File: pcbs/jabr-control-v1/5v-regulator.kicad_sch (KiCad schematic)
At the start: 0 parts

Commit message: Worked on power and other areas of the schematic
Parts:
- added C1301, C1309, C1310, C1311: 22u, Capacitor_SMD:C_0805_2012Metric, symbol Device:C_Small
- added C1302: 4u7, Capacitor_SMD:C_0805_2012Metric, symbol Device:C_Small
- added C1303, C1312: 2n2, project_footprints:C_0402, symbol Device:C_Small
- added C1304, C1306: 100n, project_footprints:C_0402, symbol Device:C_Small
- added C1305: 2u2, project_footprints:C_0402, symbol Device:C_Small
- added C1307: 1n, project_footprints:C_0402, symbol Device:C_Small
- added C1308: 4p7, project_footprints:C_0402, symbol Device:C_Small
- added C1313: 1u, project_footprints:C_0402, symbol Device:C_Small
- added D2301: PMEG4002EL-QYL, project_footprints:PMEG4002EL-QYL, symbol DIODE:PMEG4002EL-QYL
- added L1301: 74438356018, Inductor_SMD_Wurth:L_Wurth_WE-MAPI-4020, symbol PWR-IND:4020_74438356018
- added Q2602: DMN21D2UFB-7B, project_footprints:DMN21D2UFB7B, symbol MOSFET:DMN21D2UFB-7B
- added R1301, R1306: 12k1, project_footprints:R_0402, symbol Device:R_Small
- added R1302, R1308: 100k, project_footprints:R_0402, symbol Device:R_Small
- added R1303: 22k, project_footprints:R_0402, symbol Device:R_Small
- added R1304: 10k, project_footprints:R_0402, symbol Device:R_Small
- added R1305: 680R, project_footprints:R_0402, symbol Device:R_Small
- added R1307: 33k, project_footprints:R_0402, symbol Device:R_Small
- added TP1301: 1.5mm, TestPoint:TestPoint_Pad_D1.5mm, symbol Connector:TestPoint_Small
- added U1201: TPS259472ARPWR, project_footprints:TPS259472ARPWR, symbol PWR-SWCH:TPS259472ARPWR
- added U1301: MAX20004AFOC/VY+T, project_footprints:MAX20004AFOC_VY+, symbol MAX-SMPS:MAX20004AFOA_VY+T
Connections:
- new net +3V3_AON: R1302.1, R1308.1
- new net +5V: C1309.1, C1310.1, L1301.2, R1307.1, TP1301.1, U1201.6 (OUT), U1301.1 (OUT)
- new net 5V_EN: D2301.2 (A), Q2602.3 (D), R1302.2, U1301.11 (EN)
- new net BST: C1306.1, U1301.3 (BST)
- new net DVDT: C1312.1, U1201.14 (DVDT), U1201.7 (DVDT)
- new net GND: C1301.2, C1302.2, C1303.2, C1304.2, C1305.2, C1307.2, C1308.2, C1309.2, C1310.2, C1311.2, C1312.2, C1313.2, Q2602.2 (S), R1301.2, R1304.2, R1305.2, R1306.2, U1201.8 (GND), U1301.12 (SYNC), U1301.14 (GND), U1301.4 (PGND_1), U1301.5 (PGND_2), U1301.7 (PGND_3), U1301.8 (PGND_4)
- new net ILIM: R1305.1, U1201.9 (ILM)
- new net INH: D2301.1 (K), R1304.1
- new net ITIMER: C1303.1, U1201.10 (ITIMER), U1201.11 (ITIMER)
- new net LX: C1306.2, L1301.1, U1301.6 (LX)
- new net PGTH: R1306.1, R1307.2, U1201.13 (PGTH), U1201.4 (PGTH)
- new net VBUS: C1313.1, U1201.1 (EN/UVLO), U1201.12 (EN/UVLO), U1201.5 (IN)
- new net VBUS_PG: Q2602.1 (G), R1308.2, U1201.3 (PG)
- new net VIN: C1301.1, C1302.1, C1304.1, C1311.1, U1301.10 (SUP), U1301.9 (SUPSW)
- new net VIN_BIAS: C1305.1, U1301.13 (BIAS), U1301.16 (FB)
- new net VIN_COMP: C1308.1, R1303.1, U1301.15 (COMP)
- new net VIN_COMP2: C1307.1, R1303.2
- new net VIN_FOSC: R1301.1, U1301.17 (FOSC)
- no-connect marks 0 -> 2
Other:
- note added: "5V OR-ing Circuitry"
- note added: "5V Regulator"
- note added: "These components must be located on the USB-C connector side of the break line"
- note added: "VBUS eFuse"

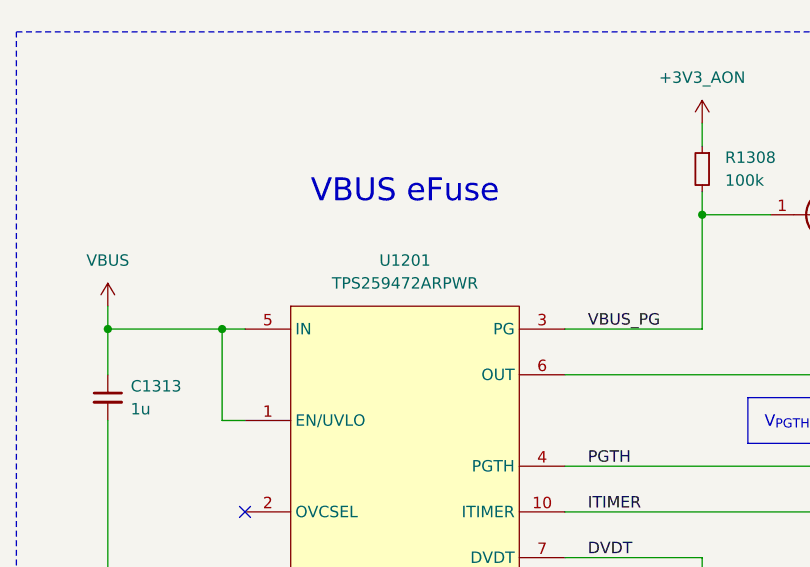
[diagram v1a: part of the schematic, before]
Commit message: Changed PCIe switch to use LQFP package
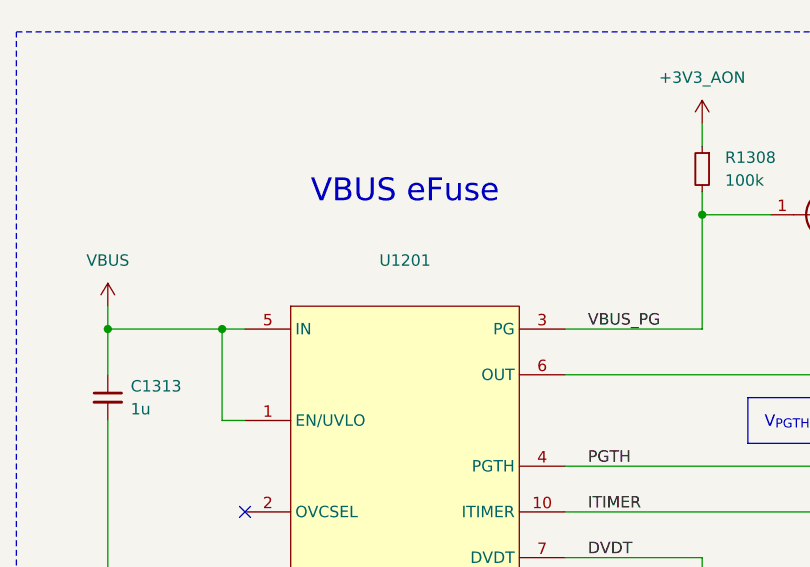
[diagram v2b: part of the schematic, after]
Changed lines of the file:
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@@
 					(size 1.27 1.27)
 				)
+				(hide yes)
 			)
 		)

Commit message: Various small updates
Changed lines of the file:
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@@
 					(size 1.27 1.27)
 				)
-				(hide yes)
 			)
 		)

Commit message: Schematic nearing completion, need to do GPIO and PHY decouplings caps
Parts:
- C1301, C1302, C1309, C1310, C1311: footprint Capacitor_SMD:C_0805_2012Metric -> project_footprints:C_0805; symbol Device:C_Small -> DEV:C_SMALL
- C1303, C1304, C1305, C1306, C1307, C1308, C1312, C1313: symbol Device:C_Small -> DEV:C_SMALL
- TP1301: footprint TestPoint:TestPoint_Pad_D1.5mm -> project_footprints:TestPoint_Pad_D1.5mm; now left out of the parts list
